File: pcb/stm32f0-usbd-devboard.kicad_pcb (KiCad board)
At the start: 2 copper layers, 30 x 42.4 mm, 24 parts, among them J1 USB_B_Mini, J2 PIN H 5P, J3 LEFT, J4 RIGHT, U1 USBLC6-2SC6, U2 MCP1700-3302E, U3 STM32F042K4T6 or STM32F042K6T6

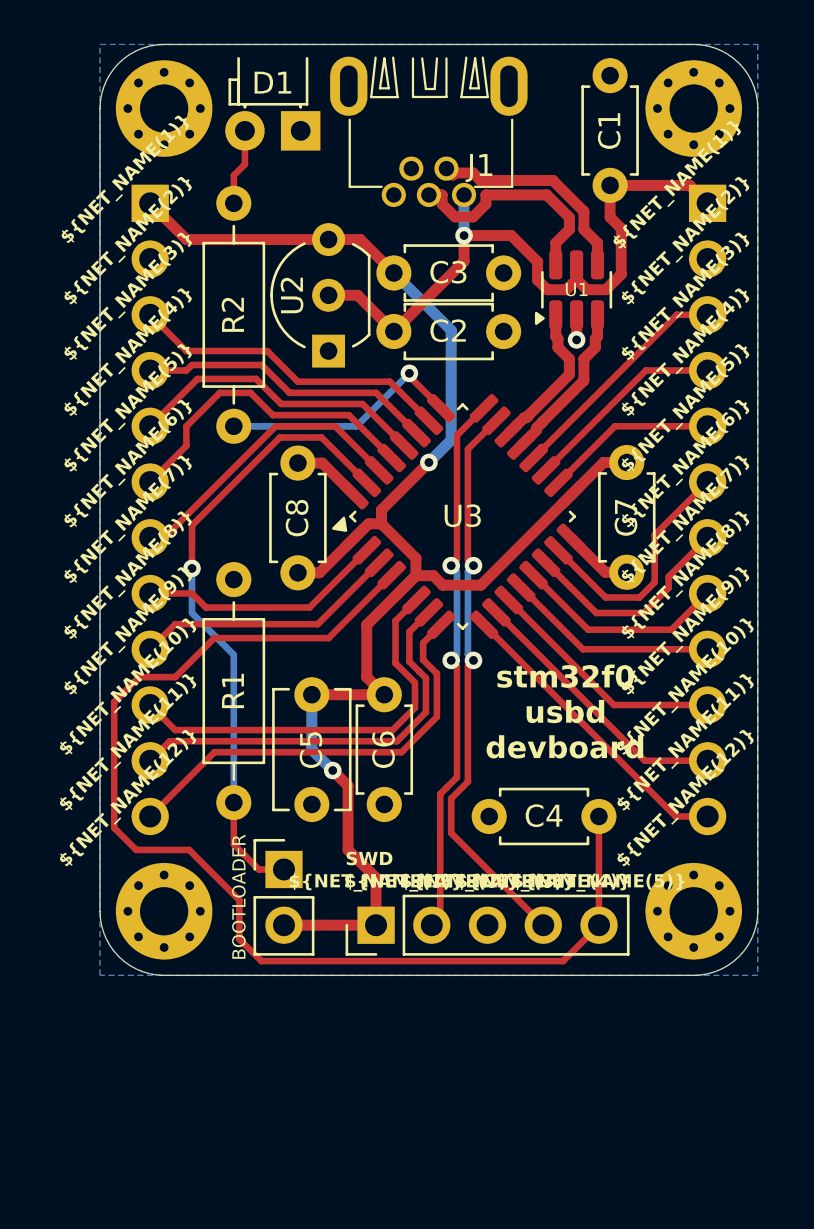
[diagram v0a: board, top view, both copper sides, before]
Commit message: pcb: revision 20241212
new protoboard-friendly pcb revision.
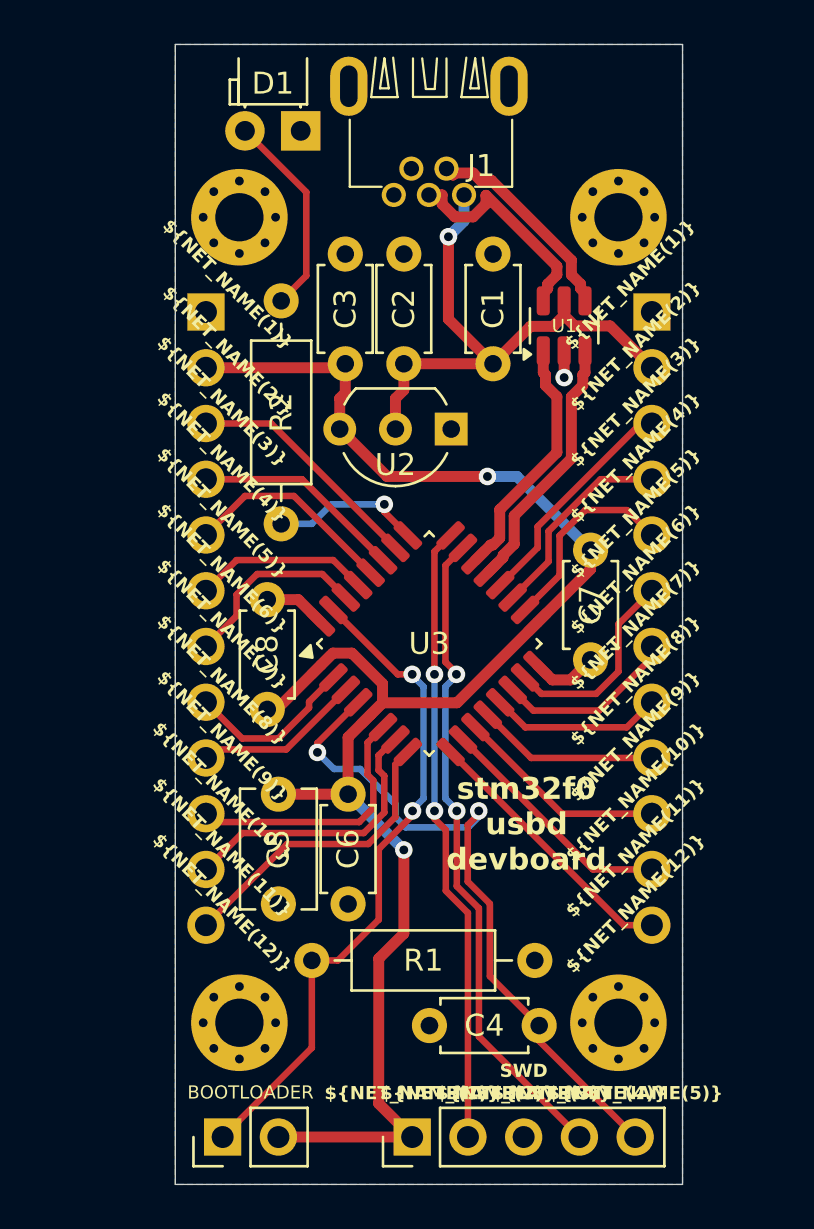
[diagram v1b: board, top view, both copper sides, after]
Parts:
- J3: footprint custom:PinHeader_DevBoard_Connector_1x12_P2.54mm_Vertical -> custom:PinHeader_DevBoard_Left_Connector_1x12_P2.54mm_Vertical
- J4: footprint custom:PinHeader_DevBoard_Connector_1x12_P2.54mm_Vertical -> custom:PinHeader_DevBoard_Right_Connector_1x12_P2.54mm_Vertical
- REF**: value OSHW-Logo2_7.3x6mm_SilkScreen -> OSHW-Symbol_6.7x6mm_SilkScreen; footprint Symbol:OSHW-Logo2_7.3x6mm_SilkScreen -> Symbol:OSHW-Symbol_6.7x6mm_SilkScreen
- moved JP1 12.5 mm to (137.7, 128.1), turned to 90 degrees
- moved C4 9.91 mm to (147.1, 123.1)
- moved J2 9.79 mm to (146.3, 128.1)
- moved C1 9.72 mm to (150.0, 87.9)
- moved REF** 8.11 mm to (147.1, 103.3)
- moved R1 8.02 mm to (141.7, 120.1), turned to 0 degrees
- moved C3 7.27 mm to (143.3, 87.9), turned to -90 degrees
- moved U2 6.62 mm to (148.1, 95.9), turned to 180 degrees
- moved C8 6.38 mm to (139.7, 103.7)
- moved H4 6.13 mm to (155.7, 122.9)
- moved H3 6.13 mm to (138.4, 122.9)
- moved H2 6.02 mm to (155.7, 86.2)
- moved H1 6.02 mm to (138.4, 86.2)
- moved U3 5.99 mm to (147.1, 105.7)
- moved C2 5.76 mm to (145.9, 87.9), turned to -90 degrees
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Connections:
- C1 pad 2: +5V -> 5V
- C2 pad 2: +5V -> 5V
- C3 pad 2: +3.3V -> 3.3V
- C5 pad 2: +3.3V -> 3.3V
- C6 pad 2: +3.3V -> 3.3V
- C7 pad 2: +3.3V -> 3.3V
- C8 pad 2: +3.3V -> 3.3V
- J1 pad 1: +5V -> 5V
- J2 pad 1: +3.3V -> 3.3V
- J3 pad 1: +3.3V -> GND
- J3 pad 2: GND -> 3.3V
- J4 pad 1: +5V -> GND
- J4 pad 2: GND -> 5V
- JP1 pad 2: +3.3V -> 3.3V
- U1 pad 5: +5V -> 5V
- U2 pad 2: +5V -> 5V
- U2 pad 3: +3.3V -> 3.3V
- U3 pad 1: +3.3V -> 3.3V
- U3 pad 17: +3.3V -> 3.3V
- U3 pad 5: +3.3V -> 3.3V
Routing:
- net 3.3V: track 0.00 -> 75.7 mm, vias 0 -> 2
- net +3.3V: track 72.8 -> 0.00 mm, vias 2 -> 0
- net +5V: track 30.4 -> 0.00 mm, vias 1 -> 0
- net 5V: track 0.00 -> 25.8 mm, vias 0 -> 1
- net NRST: track 52.1 -> 30.9 mm, vias 0 -> 2
- net A0: track 18.6 -> 12.1 mm
- net B6: track 14.4 -> 7.99 mm
- net A2: track 19.7 -> 13.9 mm
- net Net-(D1-A): track 3.51 -> 9.38 mm
- net A1: track 18.7 -> 13.0 mm
- net B7: track 13.4 -> 8.75 mm
- net USB_D+: track 6.85 -> 11.4 mm
- net USB_D-: track 7.40 -> 11.9 mm
- net F1: track 12.1 -> 7.66 mm
- net LED: track 11.2 -> 6.93 mm
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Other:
- board size 30 x 42.4 mm -> 23.1 x 51.9 mm
